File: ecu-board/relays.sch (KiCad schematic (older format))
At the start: 4 parts, among them K1 Main power relay, K2 Start motor relay

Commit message: Route almost everything.
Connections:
- net GNDS renamed GNDPWR
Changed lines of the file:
@@
 Text HLabel 4400 3400 2    50   Input ~ 0
 main_relay_input
-$Comp
-L power:GNDS #PWR028
-U 1 1 5C6C86CC
-P 3100 3450
-F 0 "#PWR028" H 3100 3200 50  0001 C CNN
-F 1 "GNDS" H 3105 3277 50  0000 C CNN
-F 2 "" H 3100 3450 50  0001 C CNN
-F 3 "" H 3100 3450 50  0001 C CNN
-	1    3100 3450
-	1    0    0    -1
-$EndComp
 Text Notes 2700 2650 0    79   ~ 16
 Main power relay
@@
 Text HLabel 6500 3400 0    50   Input ~ 0
 ~start_motor_relay_input~
+$Comp
+L power:GNDPWR #PWR?
+U 1 1 5D9BFA94
+P 3100 3450
+F 0 "#PWR?" H 3100 3250 50  0001 C CNN
+F 1 "GNDPWR" H 3104 3296 50  0000 C CNN
+F 2 "" H 3100 3400 50  0001 C CNN
+F 3 "" H 3100 3400 50  0001 C CNN
+	1    3100 3450
+	1    0    0    -1
+$EndComp
 $EndSCHEMATC

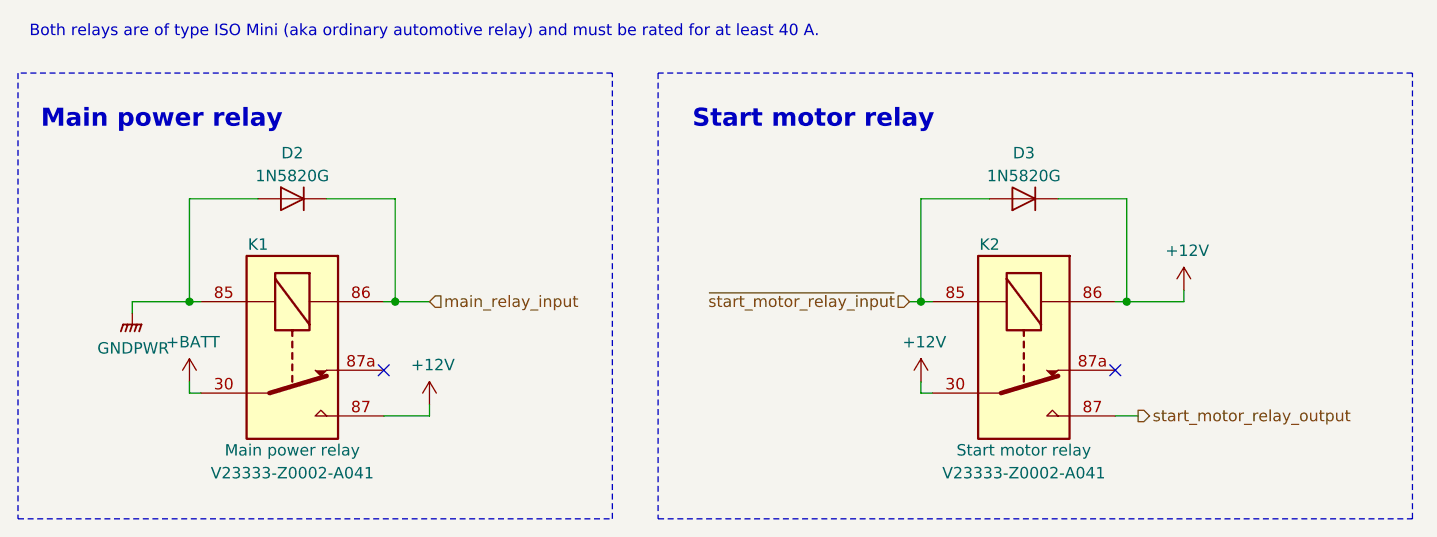
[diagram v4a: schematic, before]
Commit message: Split MicroSquirt breakout connector into three separate connectors. Old connector was impossible to route.
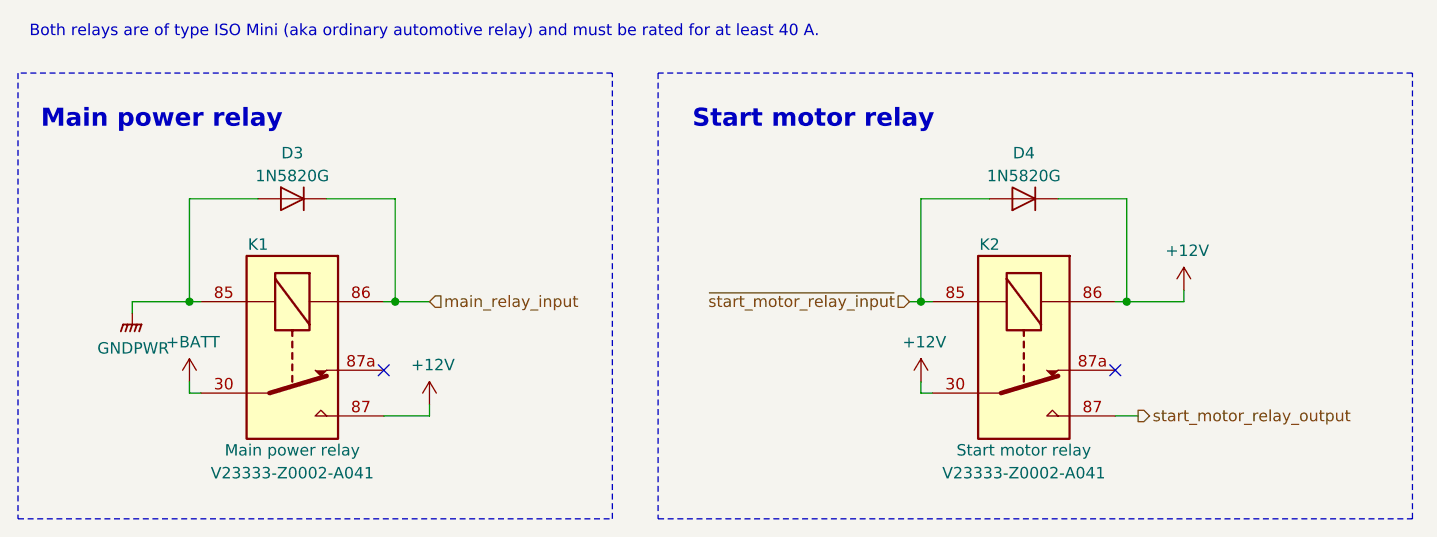
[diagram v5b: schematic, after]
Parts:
- renumbered D2 to D3, D3 to D4
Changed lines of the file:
@@
 $EndComp
 $Comp
-L Device:D D2
+L Device:D D3
 U 1 1 5C6BEE87
 P 3800 2950
-F 0 "D2" H 3800 3150 50  0000 C CNN
+F 0 "D3" H 3800 3150 50  0000 C CNN
 F 1 "1N5820G" H 3800 3050 50  0000 C CNN
 F 2 "Diodes_THT:D_A-405_P10.16mm_Horizontal" H 3800 2950 50  0001 C CNN
@@
 $EndComp
 $Comp
-L Device:D D3
+L Device:D D4
 U 1 1 5C6BEF1F
 P 7000 2950
-F 0 "D3" H 7000 2750 50  0000 C CNN
+F 0 "D4" H 7000 2750 50  0000 C CNN
 F 1 "1N5820G" H 7000 2850 50  0000 C CNN
 F 2 "Diodes_THT:D_A-405_P10.16mm_Horizontal" H 7000 2950 50  0001 C CNN
@@
 $EndComp
 $Comp
-L power:+BATT #PWR026
+L power:+BATT #PWR017
 U 1 1 5C6C2CF3
 P 3350 3750
-F 0 "#PWR026" H 3350 3600 50  0001 C CNN
+F 0 "#PWR017" H 3350 3600 50  0001 C CNN
 F 1 "+BATT" H 3365 3923 50  0000 C CNN
 F 2 "" H 3350 3750 50  0001 C CNN
@@
 NoConn ~ 7400 3700
 $Comp
-L power:+12V #PWR027
+L power:+12V #PWR018
 U 1 1 5C6C5187
 P 4400 3850
-F 0 "#PWR027" H 4400 3700 50  0001 C CNN
+F 0 "#PWR018" H 4400 3700 50  0001 C CNN
 F 1 "+12V" H 4415 4023 50  0000 C CNN
 F 2 "" H 4400 3850 50  0001 C CNN
@@
 start_motor_relay_output
 $Comp
-L power:+12V #PWR029
+L power:+12V #PWR019
 U 1 1 5C6C6B16
 P 6550 3750
-F 0 "#PWR029" H 6550 3600 50  0001 C CNN
+F 0 "#PWR019" H 6550 3600 50  0001 C CNN
 F 1 "+12V" H 6565 3923 50  0000 C CNN
 F 2 "" H 6550 3750 50  0001 C CNN
@@
 	8700 2400 5400 2400
 $Comp
-L power:+12V #PWR049
+L power:+12V #PWR020
 U 1 1 5CE305A3
 P 7700 3350
-F 0 "#PWR049" H 7700 3200 50  0001 C CNN
+F 0 "#PWR020" H 7700 3200 50  0001 C CNN
 F 1 "+12V" H 7715 3523 50  0000 C CNN
 F 2 "" H 7700 3350 50  0001 C CNN
@@
 ~start_motor_relay_input~
 $Comp
-L power:GNDPWR #PWR0101
+L power:GNDPWR #PWR016
 U 1 1 5D9BFA94
 P 3100 3450
-F 0 "#PWR0101" H 3100 3250 50  0001 C CNN
+F 0 "#PWR016" H 3100 3250 50  0001 C CNN
 F 1 "GNDPWR" H 3104 3296 50  0000 C CNN
 F 2 "" H 3100 3400 50  0001 C CNN

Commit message: Change to a larger diode footprint.
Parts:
- D3, D4: footprint Diodes_THT:D_A-405_P10.16mm_Horizontal -> Diode_THT:D_DO-201AD_P15.24mm_Horizontal
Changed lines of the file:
@@
 F 0 "D3" H 3800 3150 50  0000 C CNN
 F 1 "1N5820G" H 3800 3050 50  0000 C CNN
-F 2 "Diodes_THT:D_A-405_P10.16mm_Horizontal" H 3800 2950 50  0001 C CNN
+F 2 "Diode_THT:D_DO-201AD_P15.24mm_Horizontal" H 3800 2950 50  0001 C CNN
 F 3 "~" H 3800 2950 50  0001 C CNN
 F 4 "ON Semi" H 3800 2950 50  0001 C CNN "Manufacturer"
@@
 F 0 "D4" H 7000 2750 50  0000 C CNN
 F 1 "1N5820G" H 7000 2850 50  0000 C CNN
-F 2 "Diodes_THT:D_A-405_P10.16mm_Horizontal" H 7000 2950 50  0001 C CNN
+F 2 "Diode_THT:D_DO-201AD_P15.24mm_Horizontal" H 7000 2950 50  0001 C CNN
 F 3 "~" H 7000 2950 50  0001 C CNN
 F 4 "ON Semi" H 7000 2950 50  0001 C CNN "Manufacturer"
